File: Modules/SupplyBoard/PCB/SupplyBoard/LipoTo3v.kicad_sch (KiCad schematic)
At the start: 0 parts

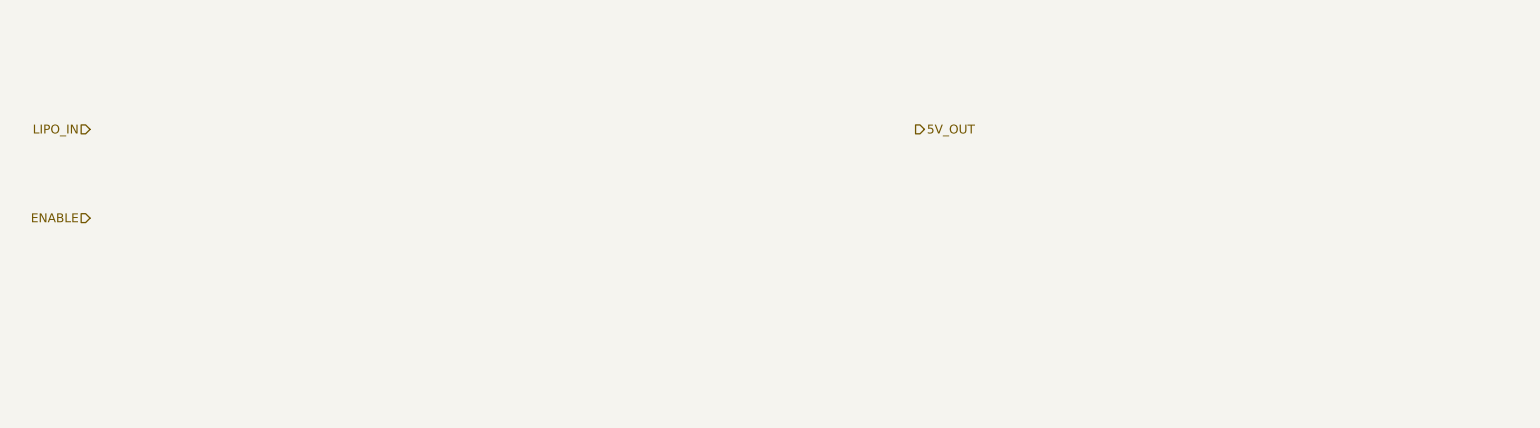
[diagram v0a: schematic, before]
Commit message: Lipo to 3v3 circuit added
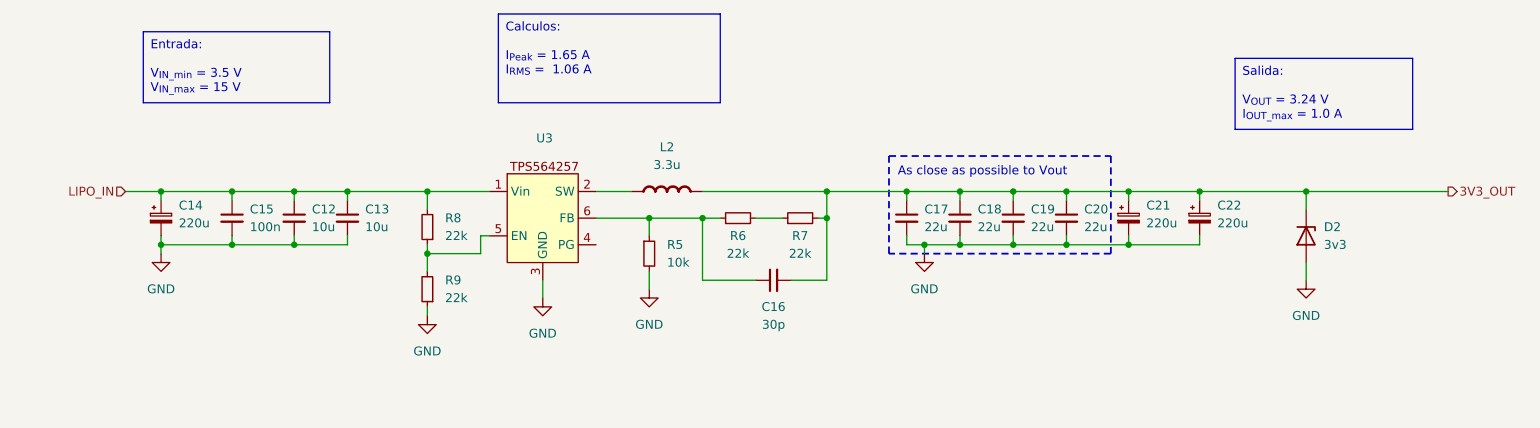
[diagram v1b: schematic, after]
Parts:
- added C12, C13: 10u, Capacitor_SMD:C_0805_2012Metric_Pad1.18x1.45mm_HandSolder, symbol Device:C_Small
- added C14, C21, C22: 220u, Capacitor_SMD:CP_Elec_6.3x5.4, symbol Device:C_Polarized_Small
- added C15: 100n, Capacitor_SMD:C_0805_2012Metric_Pad1.18x1.45mm_HandSolder, symbol Device:C_Small
- added C16: 30p, Capacitor_SMD:C_0805_2012Metric_Pad1.18x1.45mm_HandSolder, symbol Device:C_Small
- added C17, C18, C19, C20: 22u, Capacitor_SMD:C_0805_2012Metric_Pad1.18x1.45mm_HandSolder, symbol Device:C_Small
- added D2: 3v3, symbol Device:D_Zener
- added L2: 3.3u, IcaroFootprints:PSPCA_D43_Series, symbol PCM_Elektuur:L
- added R5: 10k, Resistor_SMD:R_0805_2012Metric_Pad1.20x1.40mm_HandSolder, symbol Device:R_Small
- added R6, R7, R8, R9: 22k, Resistor_SMD:R_0805_2012Metric_Pad1.20x1.40mm_HandSolder, symbol Device:R_Small
- added U3: ~, IcaroFootprints:TPS564242DRLR_TEX, symbol IcaroLib:TPS564257
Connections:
- net LIPO_IN: now also C12.1, C13.1, C14.1, C15.1, R8.2, U3.1 (Vin)
- new net: L2.1 (+), U3.2 (SW)
- new net: R8.1, R9.2, U3.5 (EN)
- new net: C16.1, R5.1, R6.1, U3.6 (FB)
- new net: R6.2, R7.1
- new net 3V3_OUT: C16.2, C17.1, C18.1, C19.1, C20.1, C21.1, C22.1, D2.1 (K), L2.2 (-), R7.2
- new net GND: C12.2, C13.2, C14.2, C15.2, C17.2, C18.2, C19.2, C20.2, C21.2, C22.2, D2.2 (A), R5.2, R9.1, U3.3 (GND)
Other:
- note added: "As close as possible to Vout"

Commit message: Changed documentation and added LCSC to buck converter
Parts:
- U3: LCSC (none) -> C19272233
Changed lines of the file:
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@@
+			)
+		)
+		(property "LCSC" "C19272233"
+			(at 143.51 81.28 0)
+			(effects
+				(font
+					(size 1.27 1.27)
+				)
+				(hide yes)
 			)
 		)

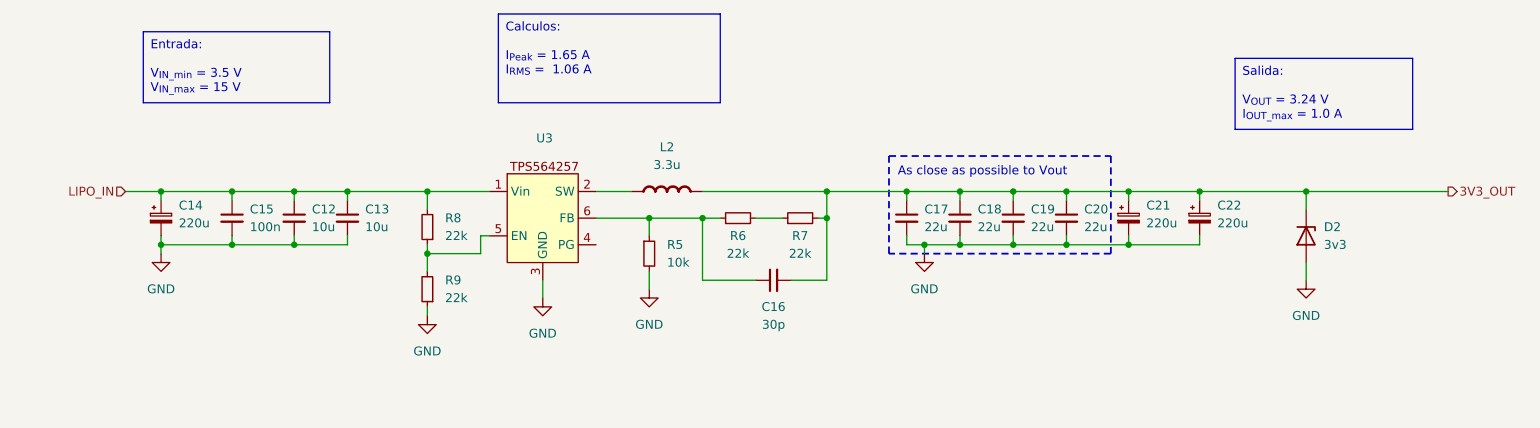
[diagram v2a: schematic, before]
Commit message: Supply board schematic and PCB
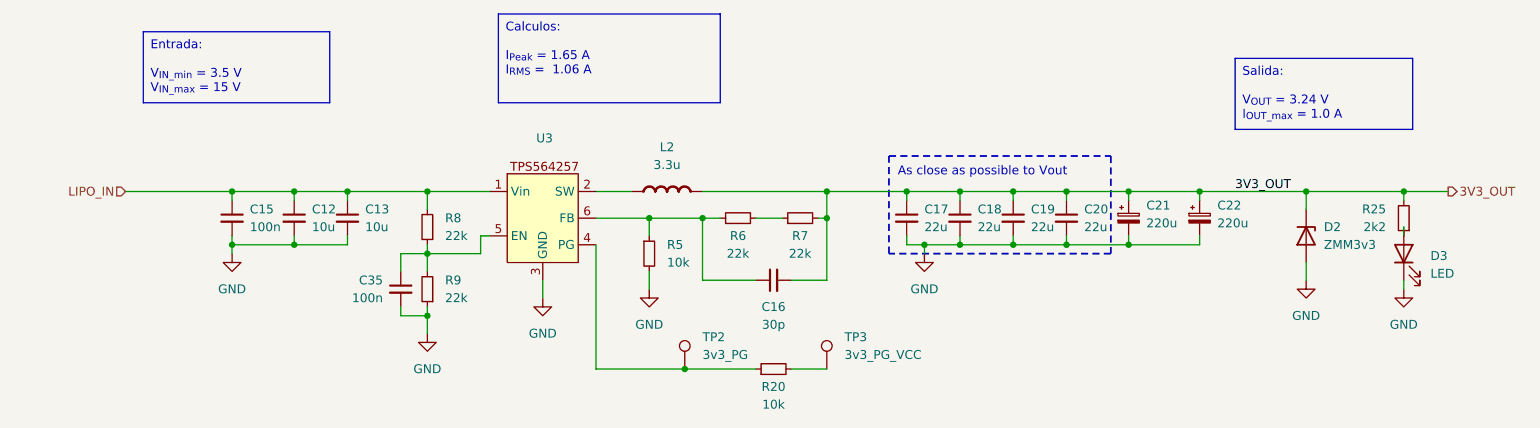
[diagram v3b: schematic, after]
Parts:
- removed C14: 220u, Capacitor_SMD:CP_Elec_6.3x5.4, symbol Device:C_Polarized_Small
- added C35: 100n, Capacitor_SMD:C_0603_1608Metric_Pad1.08x0.95mm_HandSolder, symbol Device:C_Small
- added D3: LED, LED_SMD:LED_0805_2012Metric_Pad1.15x1.40mm_HandSolder, symbol Device:LED
- added R20: 10k, Resistor_SMD:R_0603_1608Metric_Pad0.98x0.95mm_HandSolder, symbol Device:R_Small
- added R25: 2k2, Resistor_SMD:R_0603_1608Metric_Pad0.98x0.95mm_HandSolder, symbol Device:R_Small
- added TP2: 3v3_PG, TestPoint:TestPoint_Pad_D1.5mm, symbol Connector:TestPoint
- added TP3: 3v3_PG_VCC, TestPoint:TestPoint_Pad_D1.5mm, symbol Connector:TestPoint
- C12, C13, C15, C17, C18, C19, C20: footprint Capacitor_SMD:C_0805_2012Metric_Pad1.18x1.45mm_HandSolder -> Capacitor_SMD:C_0603_1608Metric_Pad1.08x0.95mm_HandSolder
- D2: value 3v3 -> ZMM3v3; footprint (none) -> Diode_SMD:D_MiniMELF
- R5, R6, R7, R8, R9: footprint Resistor_SMD:R_0805_2012Metric_Pad1.20x1.40mm_HandSolder -> Resistor_SMD:R_0603_1608Metric_Pad0.98x0.95mm_HandSolder
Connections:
- net 3V3_OUT: now also R25.2
- net GND: now also C35.2, D3.1 (K)
- net at R8.1, R9.2, U3.5 (EN): now also C35.1
- net at U3.4 (PG): now also R20.1, TP2.1
- new net: D3.2 (A), R25.1
- new net: R20.2, TP3.1

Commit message: Updated supply board for v2, and BMP280 tinkering project
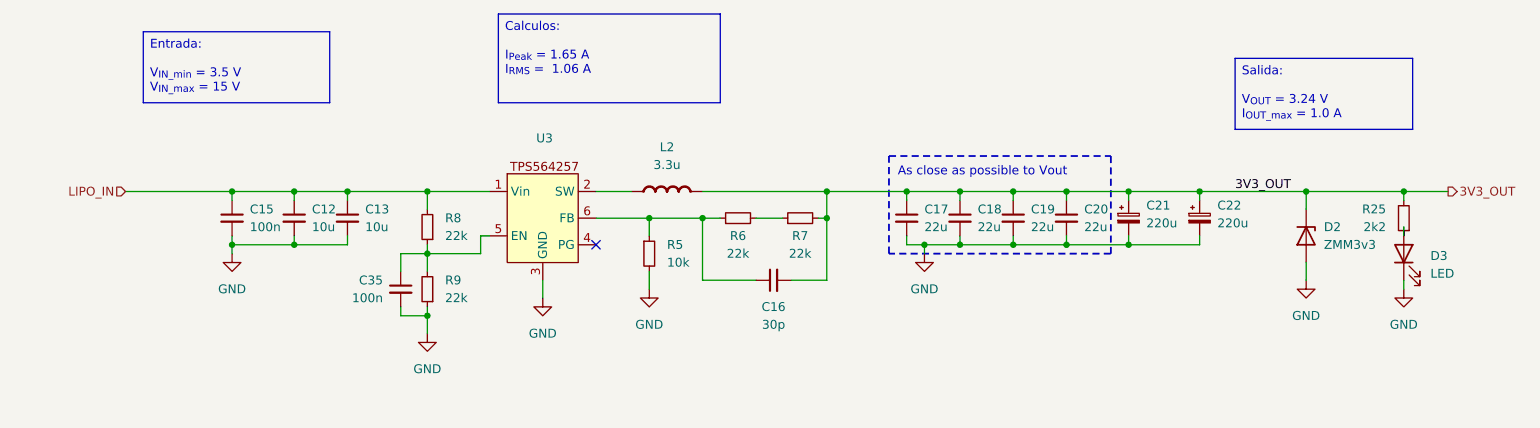
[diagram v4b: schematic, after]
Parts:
- removed R20: 10k, Resistor_SMD:R_0603_1608Metric_Pad0.98x0.95mm_HandSolder, symbol Device:R_Small
- removed TP2: 3v3_PG, TestPoint:TestPoint_Pad_D1.5mm, symbol Connector:TestPoint
- removed TP3: 3v3_PG_VCC, TestPoint:TestPoint_Pad_D1.5mm, symbol Connector:TestPoint
- C21, C22: footprint Capacitor_SMD:CP_Elec_6.3x5.4 -> Capacitor_Tantalum_SMD:CP_EIA-3216-18_Kemet-A_Pad1.58x1.35mm_HandSolder
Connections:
- no-connect marks 0 -> 1
